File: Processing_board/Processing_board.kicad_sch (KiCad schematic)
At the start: 30 parts, among them J1 Conn_01x08_Pin, J2 Conn_01x08_Pin, J3 Conn_01x06_Pin, J4 Conn_01x03_Pin, J5 Conn_01x03_Pin, J6 Conn_01x02_Pin, J7 Conn_01x02_Pin, SW1 TL3305BF100QG, SW2 TL3305BF100QG, U1 STM32WBA63CIU6

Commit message: feat: bias network, GPIO
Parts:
- added J12: Conn_01x02_Pin, symbol Connector:Conn_01x02_Pin
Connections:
- net USART1_RX: now also U1.7 (PA6); no longer U1.5 (PA8)
- net ADC_DRDY: now reaches U1.12 (PA1)
- net SPI_CS2: now reaches U1.33 (PB15)
- net ADC_GPIO2 renamed ADC/RESET
- net ADC_GPIO3 renamed ADC/START
- net SPI_*CS renamed SPI_CS1
- new net ADC/BIAS_DRV: J12.1 (Pin_1)
- new net ADC/CHREF: J12.2 (Pin_2)
- new net ADC_CLK: U1.5 (PA8)
- no-connect marks 16 -> 13
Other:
- sheet ADC ports: added BIAS_DRV, CHREF, CLK, CS1, CS2, DRDY, PWDN, RESET, START; removed *CS, GPIO2, GPIO3
- note added: "ACD_CLK"

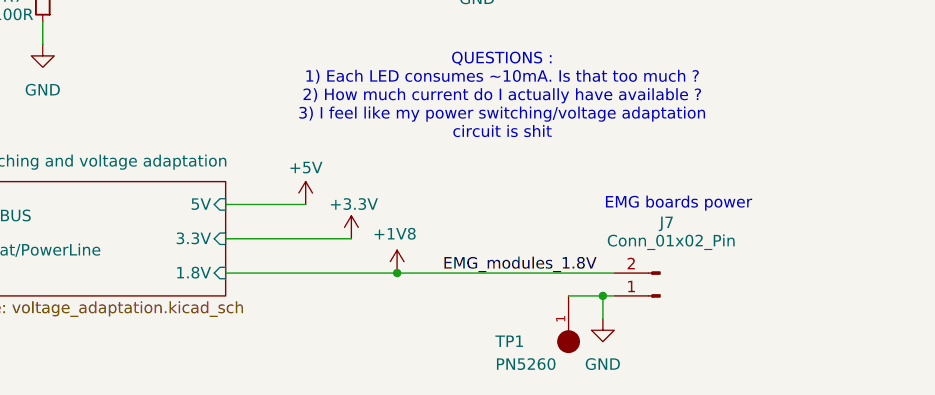
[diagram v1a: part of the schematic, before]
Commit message: Add the footprint for ADC components
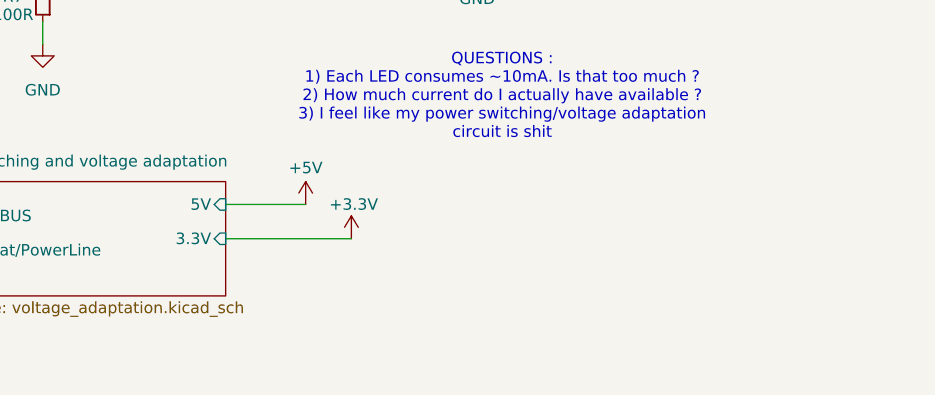
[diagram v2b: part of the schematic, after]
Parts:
- removed J7: Conn_01x02_Pin, Connector_PinSocket_2.54mm:PinSocket_1x02_P2.54mm_Vertical, symbol Connector:Conn_01x02_Pin
- removed TP1: PN5260, PN5260:PN5260, symbol PN5260:5260
- J12: footprint (none) -> Connector_PinSocket_2.54mm:PinSocket_1x02_P2.54mm_Vertical
- J6: footprint Connector_PinSocket_2.54mm:PinSocket_1x02_P2.54mm_Vertical -> Connector_JST:JST_EH_B2B-EH-A_1x02_P2.50mm_Vertical
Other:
- sheet Power switching and voltage adaptation ports: added none; removed 1.8V
- note removed: "EMG boards power"

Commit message: Changed the footprint of J6
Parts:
- J6: footprint Connector_JST:JST_EH_B2B-EH-A_1x02_P2.50mm_Vertical -> Connector_PinSocket_2.54mm:PinSocket_1x02_P2.54mm_Vertical
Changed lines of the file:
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@@
 			)
 		)
-		(property "Footprint" "Connector_JST:JST_EH_B2B-EH-A_1x02_P2.50mm_Vertical"
+		(property "Footprint" "Connector_PinSocket_2.54mm:PinSocket_1x02_P2.54mm_Vertical"
 			(at 55.88 186.69 0)
 			(effects

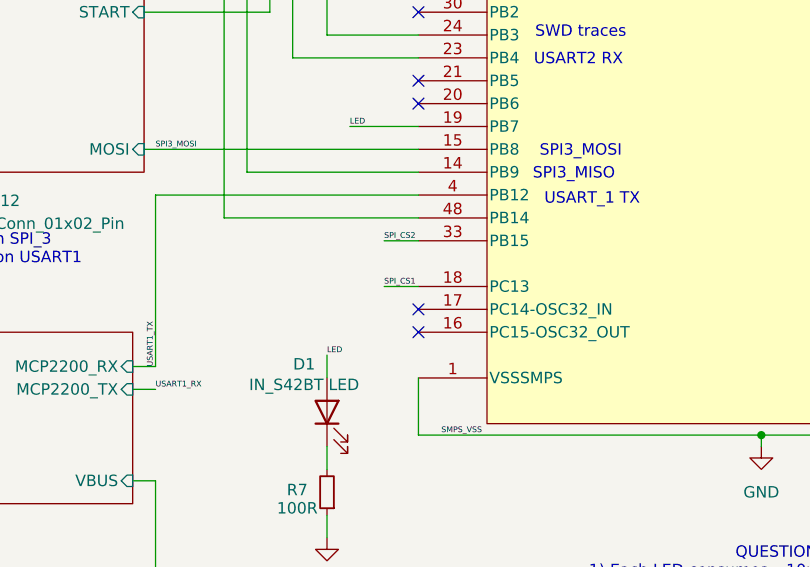
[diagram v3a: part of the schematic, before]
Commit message: feat: added all channel-resistor connections and some more stuff
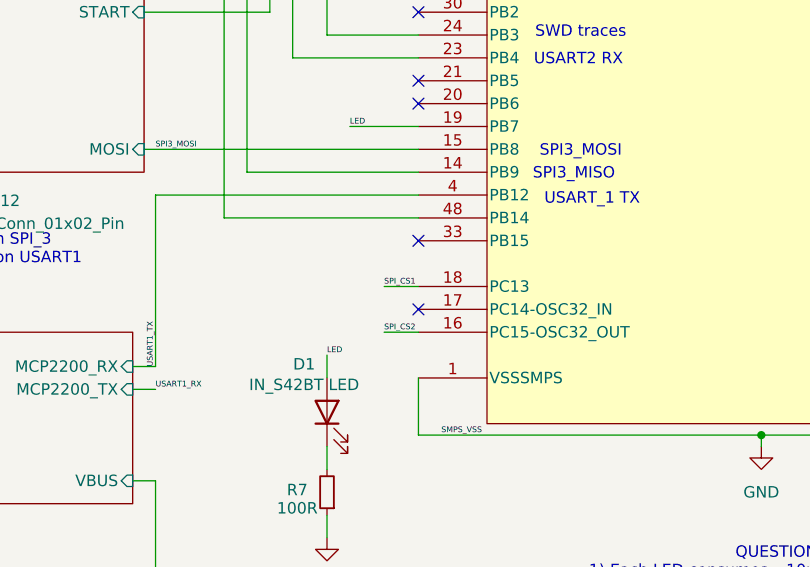
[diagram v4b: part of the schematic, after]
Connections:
- net SPI_CS2: now also U1.16 (PC15-OSC32_OUT); no longer U1.33 (PB15)
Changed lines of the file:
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@@
-	)
-	(no_connect
-		(at 105.41 138.43)
 	)
 	(no_connect
@@
 	)
 	(no_connect
+		(at 105.41 128.27)
+	)
+	(no_connect
 		(at 105.41 92.71)
 	)
@@
 	(wire
 		(pts
+			(xy 101.6 138.43) (xy 105.41 138.43)
+		)
+		(stroke
+			(width 0)
+			(type default)
+		)
+	)
+	(wire
+		(pts
 			(xy 82.55 60.96) (xy 82.55 62.23)
 		)
@@
 		(pts
 			(xy 115.57 182.88) (xy 129.54 182.88)
-		)
-		(stroke
-			(width 0)
-			(type default)
-		)
-	)
-	(wire
-		(pts
-			(xy 101.6 128.27) (xy 105.41 128.27)
 		)
 		(stroke
@@
 		)
 	)
-	(label "SPI_CS2"
-		(at 101.6 128.27 0)
-		(effects
-			(font
-				(size 0.635 0.635)
-			)
-			(justify left bottom)
-		)
-	)
 	(label "SPI3_MOSI"
 		(at 76.2 118.11 0)
@@
 		(effects
 			(font
+				(size 0.635 0.635)
+			)
+			(justify left bottom)
+		)
+	)
+	(label "SPI_CS2"
+		(at 101.6 138.43 0)
+		(effects
+			(font
